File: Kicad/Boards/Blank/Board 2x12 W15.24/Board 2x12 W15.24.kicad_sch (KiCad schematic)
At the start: 1 part, among them J1 Board 2x12 W15.24mm

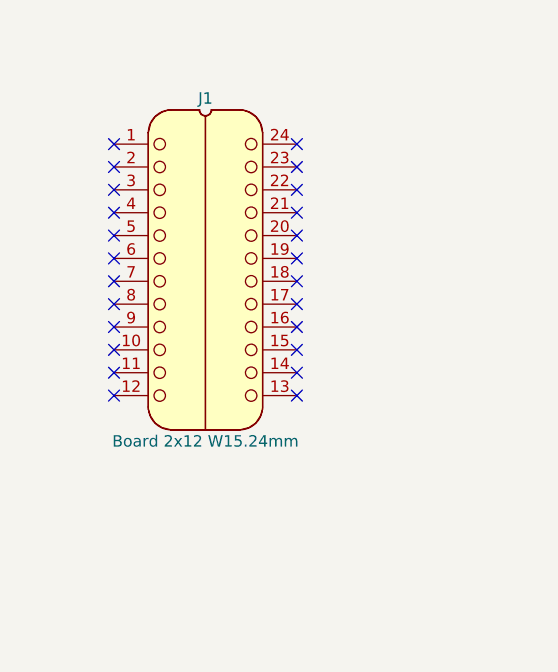
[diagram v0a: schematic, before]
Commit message: Added silkscreen and power components to some blank boards.
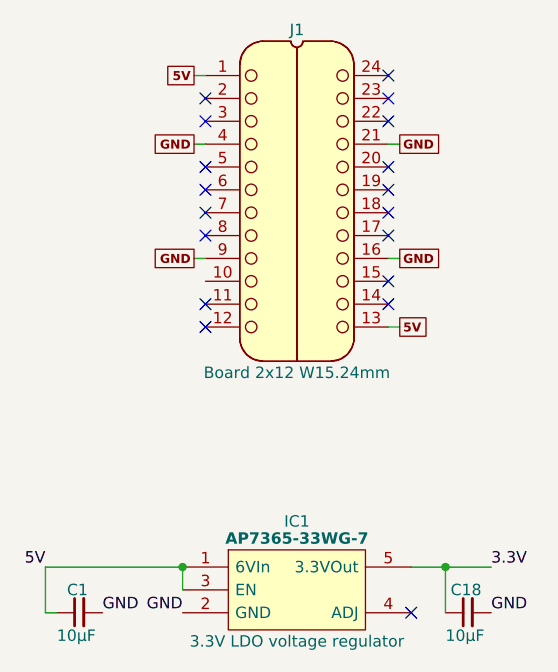
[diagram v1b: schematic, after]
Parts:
- added C1, C18: 10µF, SamacSys_Parts:C_0805, symbol HCP65:C_0805
- added IC1: AP7365-33WG-7, SamacSys_Parts:SOT95P285X130-5N, symbol Diodes_Inc:AP7365-33WG-7
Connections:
- net 5V: now reaches J1.1
- net 5V: now also J1.13, C1.1, IC1.1 (6VIn), IC1.3 (EN)
- net GND: now reaches J1.16
- net GND: now also J1.21, J1.4, J1.9, C1.2, C18.2, IC1.2 (GND)
- new net 3.3V: C18.1, IC1.5 (3.3VOut)
- no-connect marks 24 -> 18
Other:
- moved on the sheet: J1
